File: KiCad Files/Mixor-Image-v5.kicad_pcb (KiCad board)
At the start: 2 copper layers, 60.6 x 46 mm, 83 parts, among them J1 Conn_01x03_Male, J2 Conn_01x03_Female, J3 Conn_01x03_Male, J4 Conn_01x03_Female, U1 TL072, U2 TL072

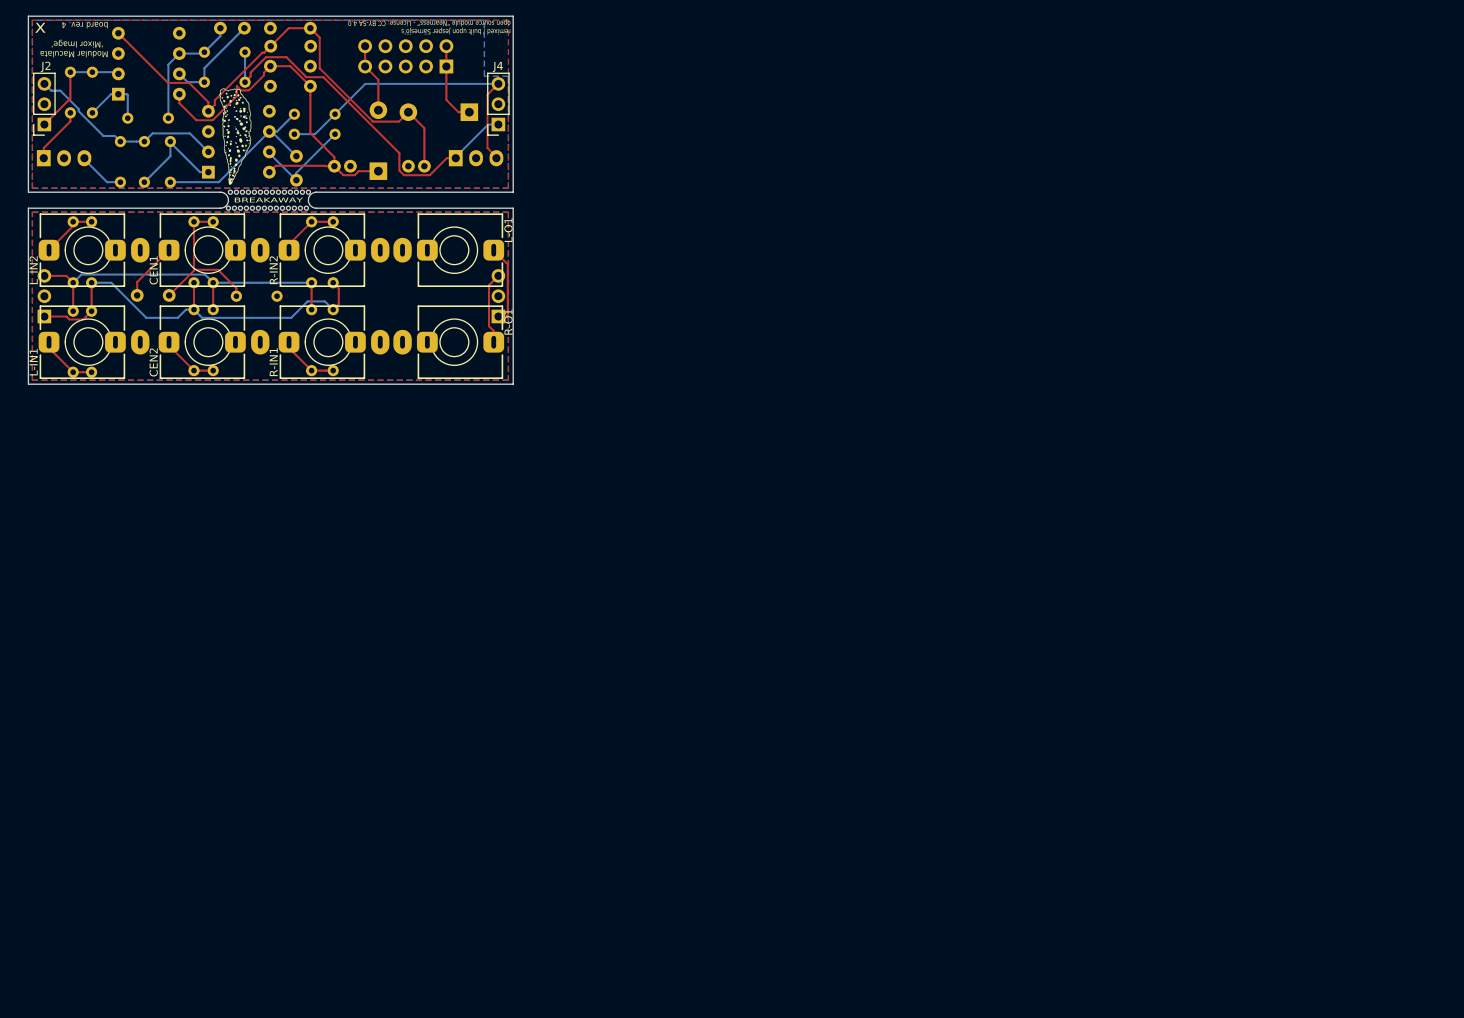
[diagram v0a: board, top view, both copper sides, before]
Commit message: remove Modular Maculata branding
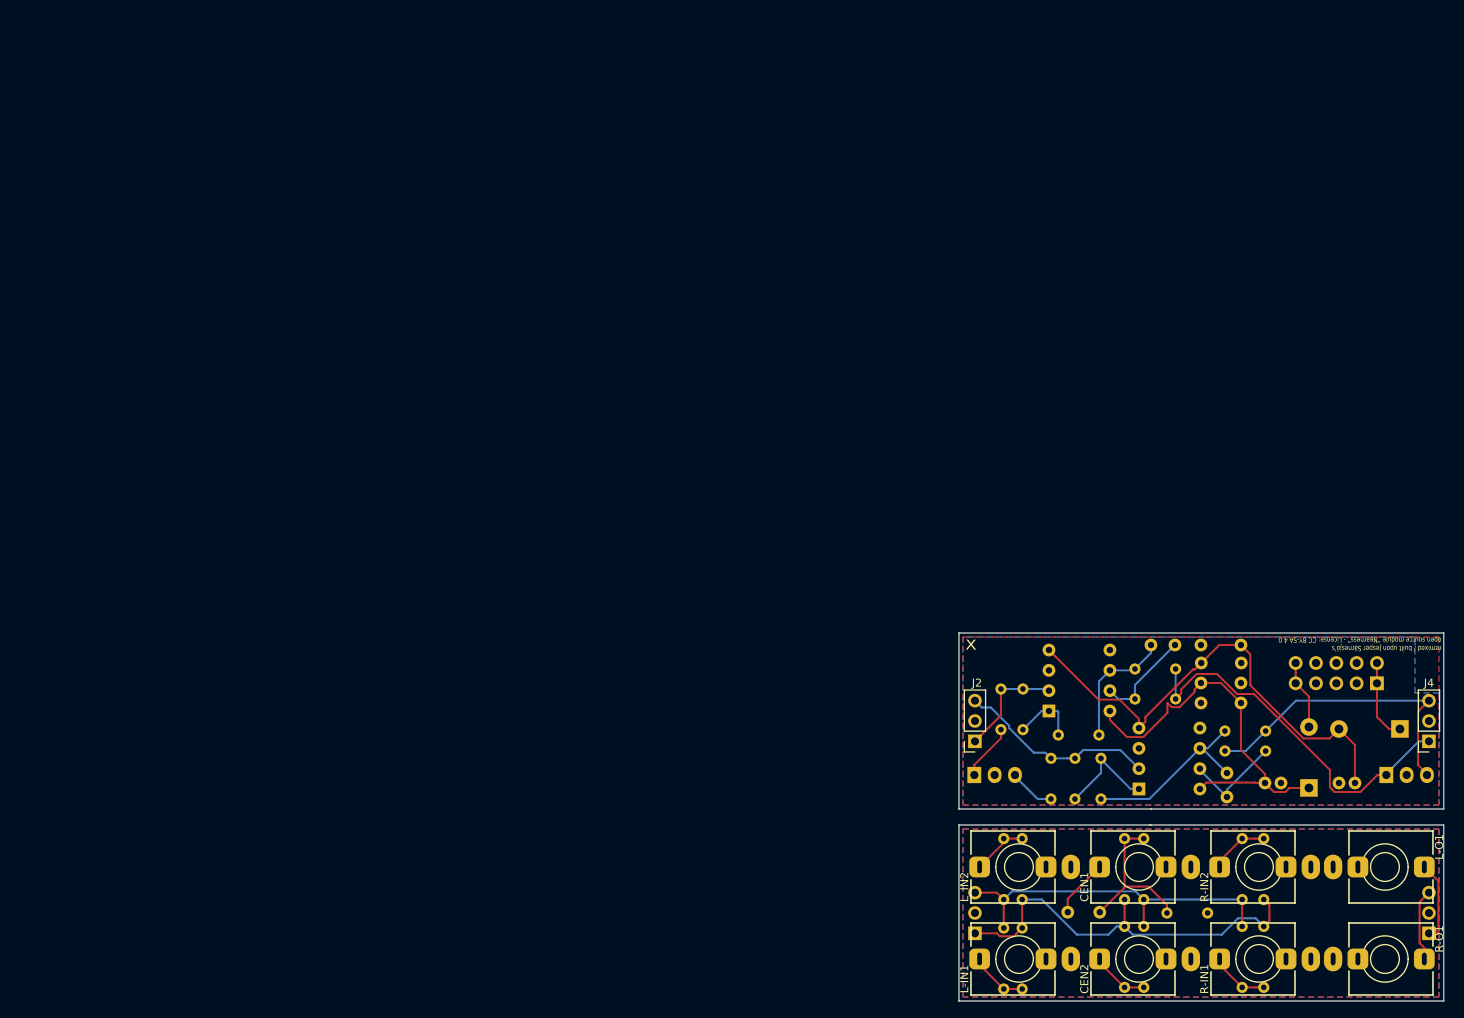
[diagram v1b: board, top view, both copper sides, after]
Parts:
- removed the G*** at (44.3, 34.3)
- removed the G*** at (26.0, 15.1)
- removed the G*** at (4.75, 3.25)
- removed REF** (x28): 0.5mm_Hole, MountingHole:MountingHole_0.5mm
- moved C1 139.6 mm to (129.9, 112.0)
- moved C7 139.6 mm to (151.6, 80.8)
- moved G*** 139.6 mm to (170.4, 106.3)
- moved R10 139.6 mm to (154.4, 121.4)
- moved R12 139.6 mm to (154.4, 102.8)
- moved R7 139.6 mm to (139.4, 102.8)
- moved R9 139.6 mm to (139.4, 121.4)
- moved J1 139.6 mm to (118.3, 114.6)
- moved J2 139.6 mm to (118.3, 90.6)
- moved L-IN1 139.6 mm to (123.8, 117.8)
- moved L_IN2 139.6 mm to (123.8, 106.3)
- moved R14 139.6 mm to (121.6, 84.1)
- moved R15 139.6 mm to (127.8, 97.8)
- moved R16 139.6 mm to (124.3, 84.1)
- moved R18 139.6 mm to (128.7, 89.8)
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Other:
- outline, holes or cut-outs redrawn
- net class Default removed
- board text removed: "BREAKAWAY"
- board text removed: "Modular Maculata ‘Mixor Image’ board rev. 4"

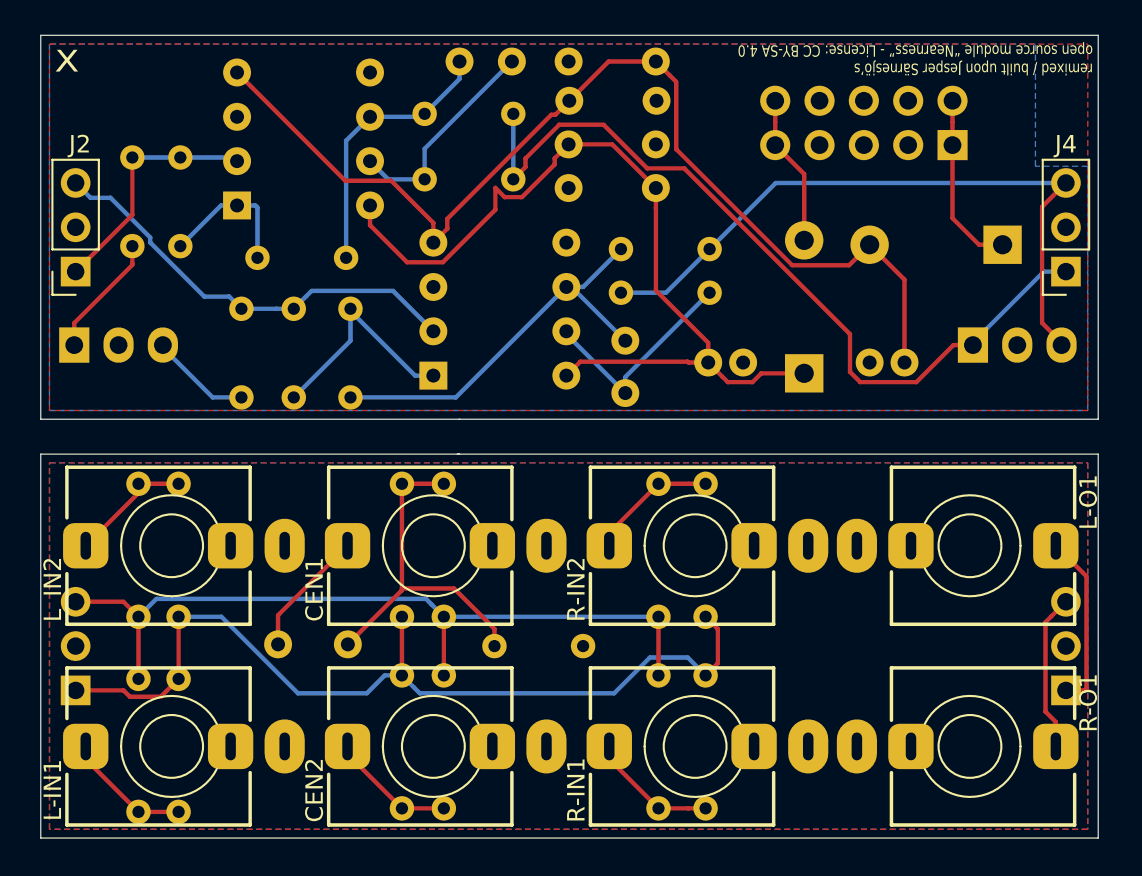
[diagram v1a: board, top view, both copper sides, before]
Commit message: only 1 error committing before flipping components so all SMD are on the same side
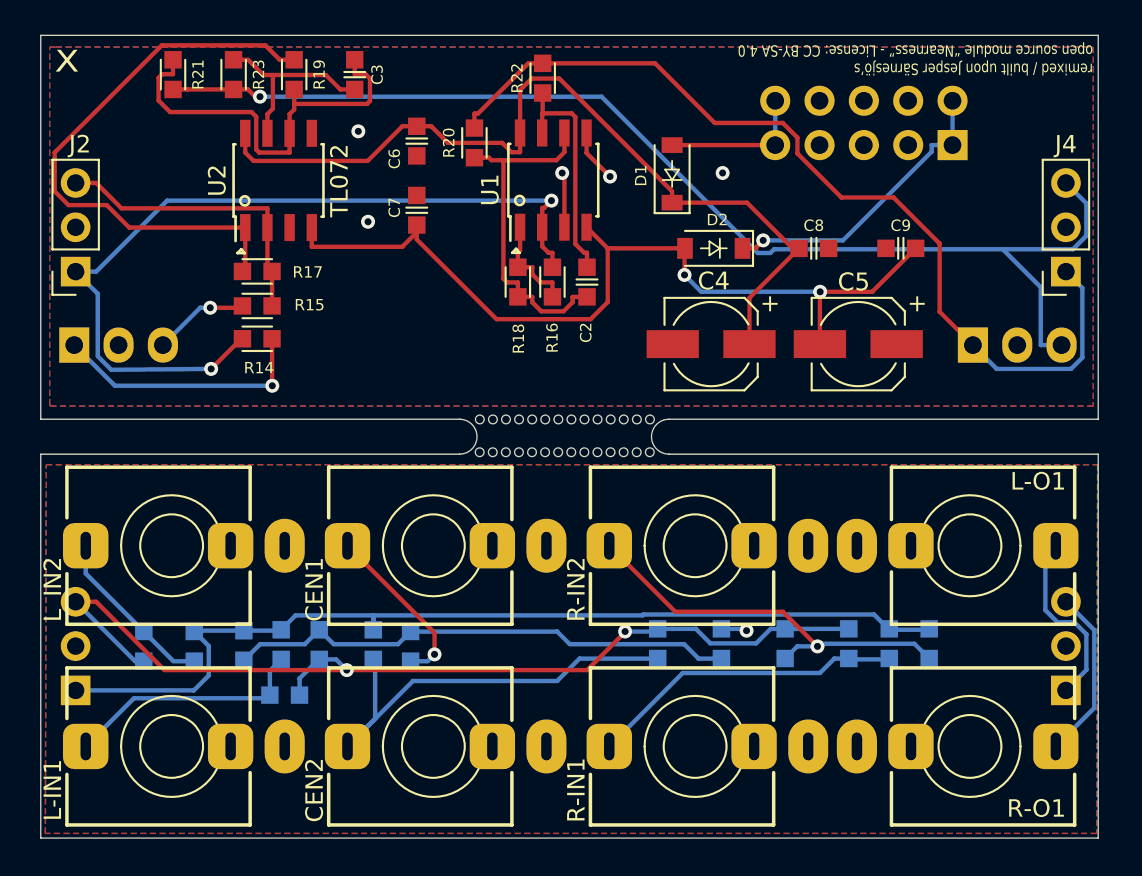
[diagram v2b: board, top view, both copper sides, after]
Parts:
- removed G***: LOGO, Nearness 1U:maculata_logo_copper
- added HOLE01: 0.5mm_Hole, MountingHole:MountingHole_0.5mm, F.Cu at (141.5, 99.1)
- added HOLE02: 0.5mm_Hole, MountingHole:MountingHole_0.5mm, F.Cu at (142.2, 99.1)
- added HOLE03: 0.5mm_Hole, MountingHole:MountingHole_0.5mm, F.Cu at (143.0, 99.1)
- added HOLE04: 0.5mm_Hole, MountingHole:MountingHole_0.5mm, F.Cu at (143.7, 99.1)
- added HOLE05: 0.5mm_Hole, MountingHole:MountingHole_0.5mm, F.Cu at (144.5, 99.1)
- added HOLE06: 0.5mm_Hole, MountingHole:MountingHole_0.5mm, F.Cu at (145.2, 99.1)
- added HOLE07: 0.5mm_Hole, MountingHole:MountingHole_0.5mm, F.Cu at (146.0, 99.1)
- added HOLE08: 0.5mm_Hole, MountingHole:MountingHole_0.5mm, F.Cu at (146.7, 99.1)
- added HOLE09: 0.5mm_Hole, MountingHole:MountingHole_0.5mm, F.Cu at (147.5, 99.1)
- added HOLE10: 0.5mm_Hole, MountingHole:MountingHole_0.5mm, F.Cu at (148.2, 99.1)
- added HOLE11: 0.5mm_Hole, MountingHole:MountingHole_0.5mm, F.Cu at (149.0, 99.1)
- added HOLE12: 0.5mm_Hole, MountingHole:MountingHole_0.5mm, F.Cu at (149.7, 99.1)
- added HOLE13: 0.5mm_Hole, MountingHole:MountingHole_0.5mm, F.Cu at (150.5, 99.1)
- added HOLE14: 0.5mm_Hole, MountingHole:MountingHole_0.5mm, F.Cu at (151.2, 99.1)
- added HOLE15: 0.5mm_Hole, MountingHole:MountingHole_0.5mm, F.Cu at (141.5, 101.0)
- added HOLE16: 0.5mm_Hole, MountingHole:MountingHole_0.5mm, F.Cu at (142.2, 101.0)
- added HOLE17: 0.5mm_Hole, MountingHole:MountingHole_0.5mm, F.Cu at (143.0, 101.0)
- added HOLE18: 0.5mm_Hole, MountingHole:MountingHole_0.5mm, F.Cu at (143.7, 101.0)
- added HOLE19: 0.5mm_Hole, MountingHole:MountingHole_0.5mm, F.Cu at (144.5, 101.0)
- added HOLE20: 0.5mm_Hole, MountingHole:MountingHole_0.5mm, F.Cu at (145.2, 101.0)
- added HOLE21: 0.5mm_Hole, MountingHole:MountingHole_0.5mm, F.Cu at (146.0, 101.0)
- added HOLE22: 0.5mm_Hole, MountingHole:MountingHole_0.5mm, F.Cu at (146.7, 101.0)
- added HOLE23: 0.5mm_Hole, MountingHole:MountingHole_0.5mm, F.Cu at (147.5, 101.0)
- added HOLE24: 0.5mm_Hole, MountingHole:MountingHole_0.5mm, F.Cu at (148.2, 101.0)
- added HOLE25: 0.5mm_Hole, MountingHole:MountingHole_0.5mm, F.Cu at (149.0, 101.0)
- added HOLE26: 0.5mm_Hole, MountingHole:MountingHole_0.5mm, F.Cu at (149.7, 101.0)
- added HOLE27: 0.5mm_Hole, MountingHole:MountingHole_0.5mm, F.Cu at (150.5, 101.0)
- added HOLE28: 0.5mm_Hole, MountingHole:MountingHole_0.5mm, F.Cu at (151.2, 101.0)
- C1: footprint Capacitor_THT:C_Rect_L4.0mm_W2.0mm_P4.00mm -> 4ms/4ms-kicad-lib/footprints/4ms_Capacitor.pretty:C_0603
- C2, C3: footprint Capacitor_THT:C_Disc_D4.0mm_W1.6mm_P3.0mm -> 4ms/4ms-kicad-lib/footprints/4ms_Capacitor.pretty:C_0603; moved to F.Cu
- C4, C5: footprint Capacitor_THT:C_Radial_D5.0mm_H11.0mm_P2.00mm -> 4ms/4ms-kicad-lib/footprints/4ms_Capacitor.pretty:CP_Elec_5x5.3; moved to F.Cu
- C6, C7, C8, C9: footprint Capacitor_THT:C_Disc_D4.3mm_W1.9mm_P5.00mm -> 4ms/4ms-kicad-lib/footprints/4ms_Capacitor.pretty:C_0603; moved to F.Cu
- D1, D2: footprint Diode_THT:D_DO-41_SOD81_P7.62mm_Horizontal -> 4ms/4ms-kicad-lib/footprints/4ms_Diode.pretty:D_SOD-123; moved to F.Cu
- R1: footprint Resistor_THT:R_Axial_DIN0204_L3.6mm_D1.6mm_P5.08mm_Horizontal -> 4ms/4ms-kicad-lib/footprints/4ms_Resistor.pretty:R_0603
- R10, R11, R12, R13, R2, R3, R4, R5, R6, R7, R8, R9: footprint Resistor_THT:R_Axial_DIN0204_L3.6mm_D1.6mm_P7.62mm_Horizontal -> 4ms/4ms-kicad-lib/footprints/4ms_Resistor.pretty:R_0603
- R14, R15, R16, R17, R18, R19, R20, R21, R22, R23: footprint Resistor_THT:R_Axial_DIN0204_L3.6mm_D1.6mm_P5.08mm_Horizontal -> 4ms/4ms-kicad-lib/footprints/4ms_Resistor.pretty:R_0603; moved to F.Cu
- U1, U2: footprint Package_DIP:DIP-8_W7.62mm_Socket -> 4ms/4ms-kicad-lib/footprints/4ms_Package_SOIC.pretty:SOIC-8_3.9x4.9mm_Pitch1.27mm; moved to F.Cu
- moved R23 30.0 mm to (127.4, 79.3), turned to -90 degrees
- moved R21 27.5 mm to (123.9, 79.3), turned to -90 degrees
- moved R16 22.5 mm to (145.6, 91.2)
- moved C9 21.8 mm to (165.6, 89.3)
- moved C3 21.7 mm to (134.3, 79.3)
- moved U1 18.2 mm to (145.7, 85.4), turned to 90 degrees
- moved D2 16.6 mm to (154.9, 89.3)
- moved R12 15.8 mm to (167.2, 112.0), turned to 90 degrees
- moved R9 15.5 mm to (151.7, 112.0)
- moved C8 15.3 mm to (160.6, 89.3)
- moved C7 15.1 mm to (137.9, 87.1), turned to -90 degrees
- moved R18 15.0 mm to (143.7, 91.2), turned to -90 degrees
- moved C2 14.6 mm to (147.6, 91.2), turned to 90 degrees
- moved R11 14.4 mm to (162.6, 112.0)
- moved U2 14.3 mm to (129.9, 85.4), turned to 90 degrees
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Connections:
- L-O1 pad TN: Net-(L-O1-PadTN) -> unconnected-(L-O1-PadTN)
- R-O1 pad TN: Net-(R-O1-PadTN) -> unconnected-(R-O1-PadTN)
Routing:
- net Net-(J2-Pin_1): track 14.0 -> 48.2 mm, vias 0 -> 2
- net Net-(J4-Pin_3): track 38.4 -> 68.4 mm, vias 0 -> 1
- net Net-(R17-Pad2): track 12.8 -> 33.2 mm
- net Net-(CEN2-PadT): track 7.24 -> 25.7 mm
- net Net-(R-IN2-PadT): track 7.42 -> 23.3 mm, vias 0 -> 1
- net Net-(J1-Pin_3): track 44.9 -> 58.6 mm, vias 0 -> 2
- net -12V: track 60.7 -> 50.0 mm, vias 0 -> 2
- net Net-(R-IN1-PadT): track 7.42 -> 18.2 mm
- net Net-(C1-Pad2): track 20.1 -> 29.4 mm
- net Net-(ST-IN1-Pin_1): track 7.05 -> 15.1 mm, vias 0 -> 1
- net Net-(J2-Pin_3): track 25.0 -> 17.3 mm
- net GND: track 0.00 -> 7.70 mm, vias 0 -> 6
- net Net-(D2-K): track 10.2 -> 17.3 mm, vias 0 -> 1
- net Net-(L-IN1-PadT): track 7.30 -> 14.2 mm
- net Net-(J4-Pin_1): track 47.1 -> 52.5 mm
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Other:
- outline, holes or cut-outs redrawn
